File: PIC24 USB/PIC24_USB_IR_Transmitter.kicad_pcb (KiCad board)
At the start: 2 copper layers, 86.4 x 48.3 mm, 56 parts, among them CON1 USB-MINI-B, P1 CONN_6, P2 CONN_4, P3 CONN_4, P4 CONN_8, P5 CONN_4, P6 CONN_1, P7 CONN_8, P8 CONN_8X2, Q1 2N7002, Q2 2N7002, Q3 2N7002, Q4 2N7002, Q5 2N7002, Q6 2N7002, U1 PIC24FJXXXGB106, U2 LM1117_SOT223_3V3, U3 50mm_5x7_Dot_Matrix_Led_Displ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, U4 MCP48X2, U5 MCP9700, X1 CRYSTAL_12MHZ, X2 32khz

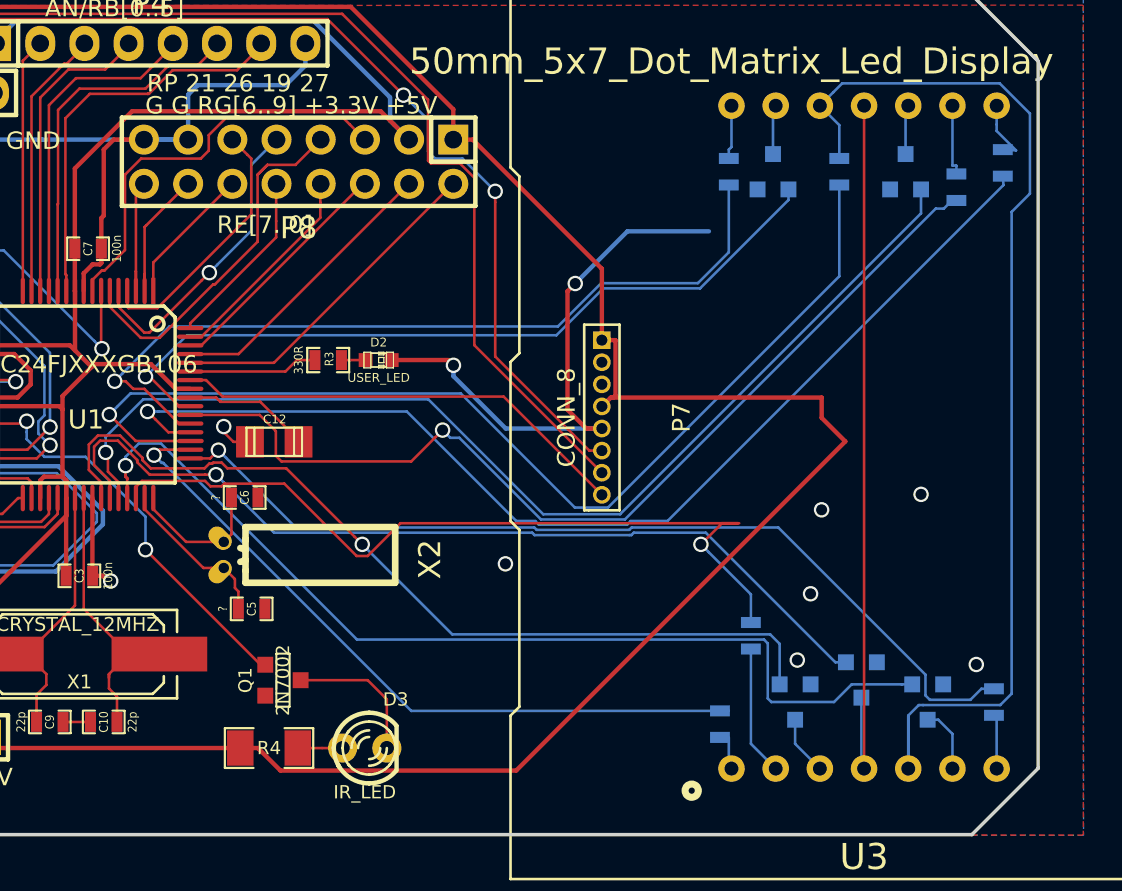
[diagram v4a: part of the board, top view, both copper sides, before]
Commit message: changes in the led matrix routing connections
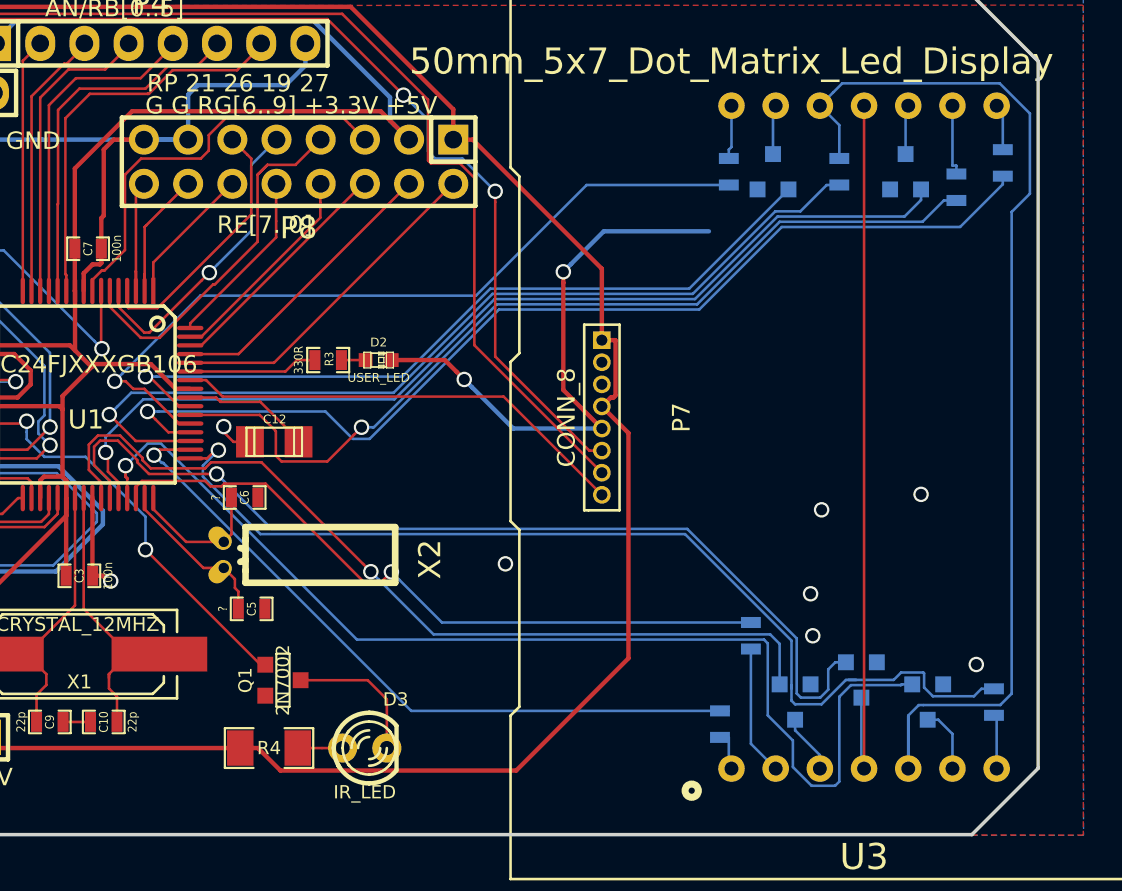
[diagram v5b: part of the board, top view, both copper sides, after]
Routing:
- net +5V: track 235.5 -> 218.0 mm
- net /MCUSection/PORTD3: track 61.9 -> 53.4 mm
- net /Dot Matrix Sheet/C5: track 58.5 -> 66.5 mm
- net /MCUSection/PORTD0: track 46.5 -> 40.2 mm
- net /Dot Matrix Sheet/C4: track 63.5 -> 57.6 mm
- net /MCUSection/PORTD1: track 53.4 -> 59.2 mm
- net /MCUSection/PORTD6: track 56.4 -> 52.2 mm
- net /MCUSection/PORTD4: track 63.4 -> 59.3 mm
- net /Dot Matrix Sheet/C3: track 52.1 -> 56.3 mm
- net /MCUSection/PORTD5: track 47.6 -> 45.3 mm
- net Net-(R12-Pad1): track 3.79 -> 2.67 mm

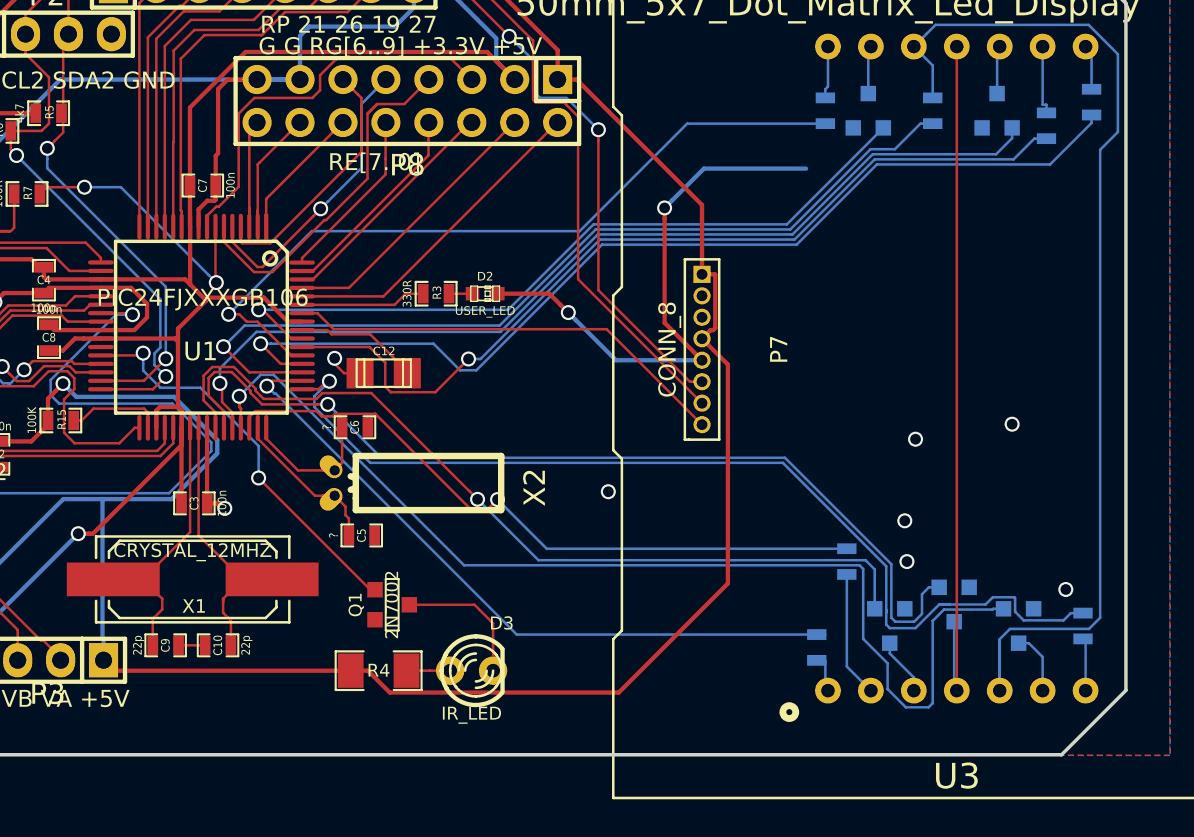
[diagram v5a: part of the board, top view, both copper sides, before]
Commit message: added I2C Temp sensor and eeprom
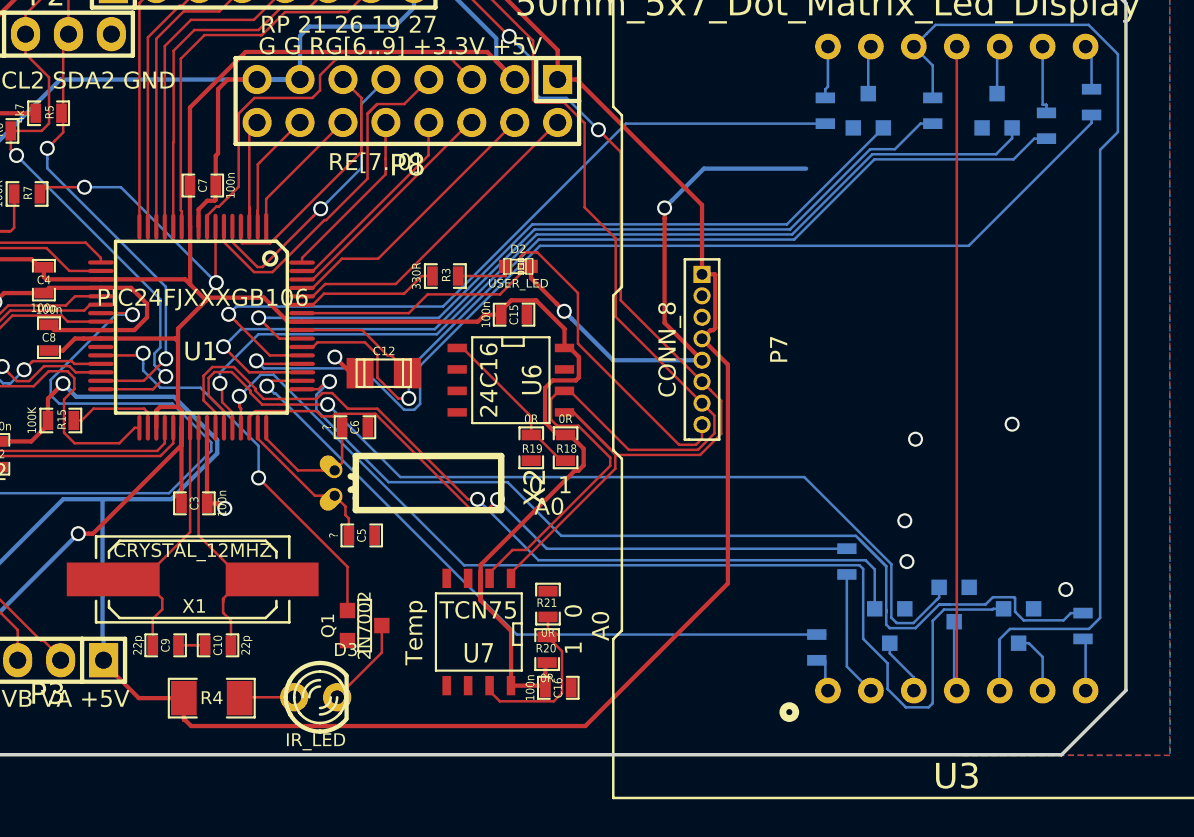
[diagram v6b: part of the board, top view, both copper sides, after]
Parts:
- added C15: 100n, SMD_Packages:SMD-0603_c, F.Cu at (74.3, 34.9)
- added C16: 100n, SMD_Packages:SMD-0603_c, F.Cu at (76.9, 57.0)
- added R18: 0R, SMD_Packages:SMD-0603_r, F.Cu at (77.3, 42.8)
- added R19: 0R, SMD_Packages:SMD-0603_r, F.Cu at (75.3, 42.8)
- added R20: 0R, SMD_Packages:SMD-0603_r, F.Cu at (76.3, 54.7)
- added R21: 0R, SMD_Packages:SMD-0603_r, F.Cu at (76.3, 52.0)
- added U6: 24C16, SMD_Packages:SOIC-8-N, F.Cu at (74.1, 38.8)
- added U7: TCN75, SMD_Packages:SOIC-8-N, F.Cu at (72.2, 53.7)
- moved R4 10.0 mm to (56.4, 57.6)
- moved D3 9.36 mm to (62.6, 57.6)
- moved D2 2.54 mm to (74.5, 32.1)
- moved Q1 2.04 mm to (65.5, 53.3)
- moved R3 1.18 mm to (70.2, 32.6)
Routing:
- net +3.3V: track 191.0 -> 241.7 mm
- net SCL: track 92.3 -> 122.3 mm
- net SDA: track 85.2 -> 112.6 mm
- net Net-(R20-Pad2): track 0.00 -> 10.1 mm
- net Net-(R18-Pad2): track 0.00 -> 9.81 mm
- net ~LCD_RESET~: track 26.4 -> 33.2 mm
- net +5V: track 218.0 -> 221.3 mm
- net Net-(D3-Pad2): track 8.29 -> 5.34 mm
- net /MCUSection/PORTD4: track 59.3 -> 62.2 mm
- net Net-(D2-Pad1): track 1.39 -> 3.36 mm
- net /MCUSection/PORTD1: track 59.2 -> 60.9 mm
- net /MCUSection/PORTD6: track 52.2 -> 53.7 mm
- net GND: track 138.4 -> 137.3 mm
- net /MCUSection/RF1: track 7.44 -> 8.42 mm
- net Net-(D3-Pad1): track 2.58 -> 3.25 mm
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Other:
- board text added: "0 1"
- board text added: "1 0 A0"
- board text added: "A0"
- board text added: "Temp"
